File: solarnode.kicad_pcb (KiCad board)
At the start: 2 copper layers, 35.9 x 42.4 mm, 85 parts, among them J1 Conn_01x06, J2 Conn_01x02, J3 Conn_01x02, J4 Conn_01x02, Q1 AO3400, Q4 S8550, Q5 S8050, SW1 3*4*2mm, U1 LM358, U2 OC5864, U3 PY32F003F18U6TR, U4 MAX485E, U5 SGM2033-3.3

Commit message: 设置最小走线宽度，添加一个覆铜区域
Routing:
- added copper zone on F.Cu, net /SLR+
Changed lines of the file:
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@@
+	)
+	(zone
+		(net 2)
+		(net_name "/SLR+")
+		(layer "F.Cu")
+		(hatch edge 0.5)
+		(priority 2)
+		(connect_pads
+			(clearance 0.5)
+		)
+		(min_thickness 0.25)
+		(filled_areas_thickness no)
+		(fill
+			(thermal_gap 0.5)
+			(thermal_bridge_width 0.5)
+		)
+		(polygon
+			(pts
+				(xy 120.72 74.08) (xy 125.07 74.07) (xy 125.07 77.51) (xy 124.13 77.51)
+			)
+		)
 	)
 	(zone
@@
 		(members "0b195e1f-babf-4dd7-9778-632fff0e3cce" "0b9fd526-c495-4a28-b2e9-279cccde64c3"
 			"0cb29699-525d-4bef-8c6a-afe7e7c22e20" "10d58e8f-0aad-4bec-bd13-2f00d2747619"
-			"1c242126-39b0-447e-830a-f3419bd5cad9" "25452366-fbd4-4985-bb02-c5ece706e4f4"
-			"27b9df76-6cdb-48db-b4f1-e2f8790ba447" "28aaa7e5-87bc-432f-b25e-acfecf6c6762"
-			"2f6ba13a-da92-4fc3-804b-7dc0fc54600a" "3cfbca58-6908-402c-8276-13622b5ffac9"
-			"4275d5b1-ca27-4961-b031-94b2a6b556a3" "452a51fe-f178-469a-a51a-106b8d1dc850"
-			"51f7e861-3757-4698-89f5-b66a34f994b3" "58c3f5fa-2f3d-4d57-825c-d2c1d860c3b2"
-			"5941b24d-1f63-45ff-967a-e51922289169" "5a586efe-4cbd-4fc6-b4a6-e8dbcd59427e"
-			"5f12d628-a1dd-4db5-938a-4d464c3aa2ad" "6415759b-c2e6-4038-8d28-fc3f17af7cc9"
-			"6ba225a6-c6fd-4747-89fa-a114a3a3d984" "6f81ba97-3f2b-443c-96c2-e10cbbdcc9ac"
-			"7b04d5f7-4c74-4899-b87d-20ca741adffe" "7fd1d17c-de07-4936-b434-a1391bb95d6b"
+			"1c242126-39b0-447e-830a-f3419bd5cad9" "204c7967-4432-440b-a5a2-ccb7b2b515f3"
+			"25452366-fbd4-4985-bb02-c5ece706e4f4" "27b9df76-6cdb-48db-b4f1-e2f8790ba447"
+			"28aaa7e5-87bc-432f-b25e-acfecf6c6762" "2f6ba13a-da92-4fc3-804b-7dc0fc54600a"
+			"3cfbca58-6908-402c-8276-13622b5ffac9" "4275d5b1-ca27-4961-b031-94b2a6b556a3"
+			"452a51fe-f178-469a-a51a-106b8d1dc850" "51f7e861-3757-4698-89f5-b66a34f994b3"
+			"58c3f5fa-2f3d-4d57-825c-d2c1d860c3b2" "5941b24d-1f63-45ff-967a-e51922289169"
+			"5a586efe-4cbd-4fc6-b4a6-e8dbcd59427e" "5f12d628-a1dd-4db5-938a-4d464c3aa2ad"
+			"6415759b-c2e6-4038-8d28-fc3f17af7cc9" "6ba225a6-c6fd-4747-89fa-a114a3a3d984"
+			"6f81ba97-3f2b-443c-96c2-e10cbbdcc9ac" "7b04d5f7-4c74-4899-b87d-20ca741adffe"
+			"7fd1d17c-de07-4936-b434-a1391bb95d6b" "804d4bcb-e463-4575-b1d0-e9075123a17c"
 			"80c44cac-9446-4b06-b20b-3ae549fe4b68" "88546c8c-a9af-4307-93a9-23e95cf7837e"
 			"8cda7904-a0ac-4ade-8034-a40ec37bfcb2" "ae562753-035c-49e5-87da-800e1a1d988c"

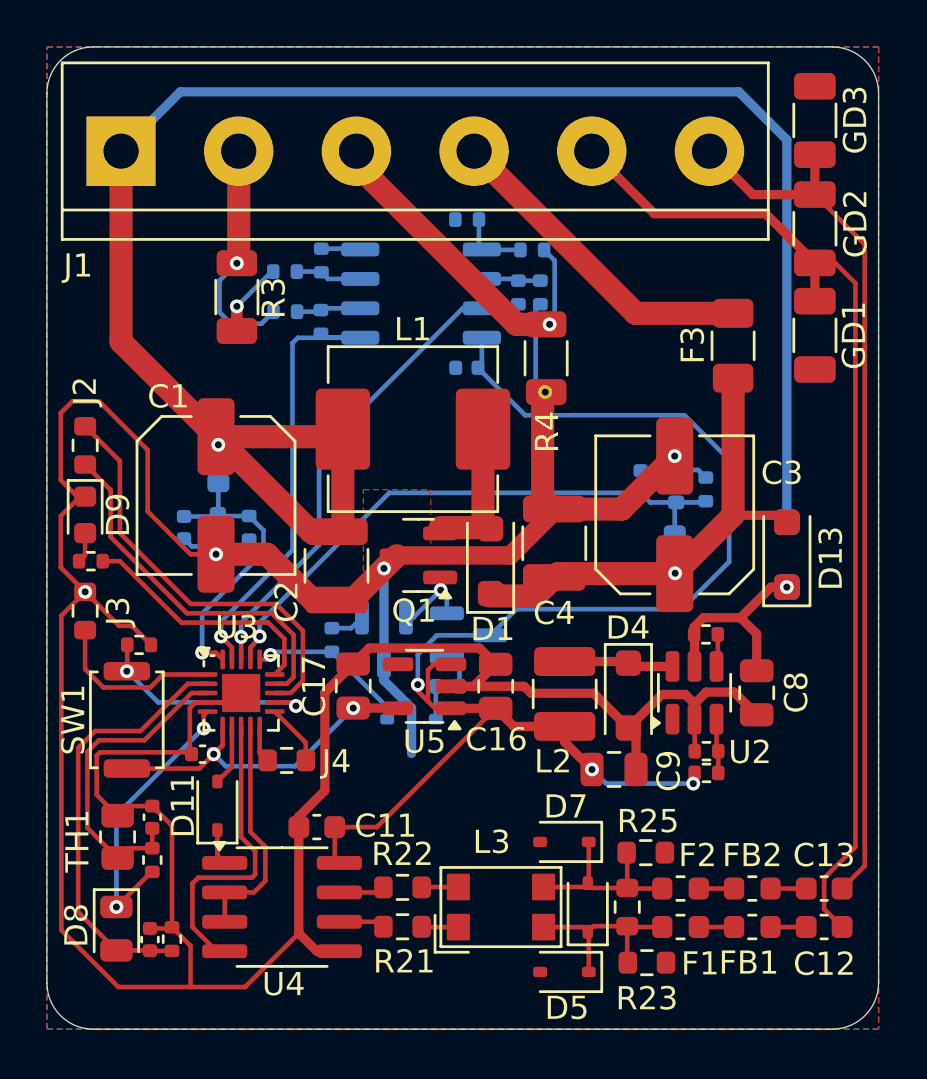
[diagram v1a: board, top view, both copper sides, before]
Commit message: 优化GND连接，添加过孔，调整走线
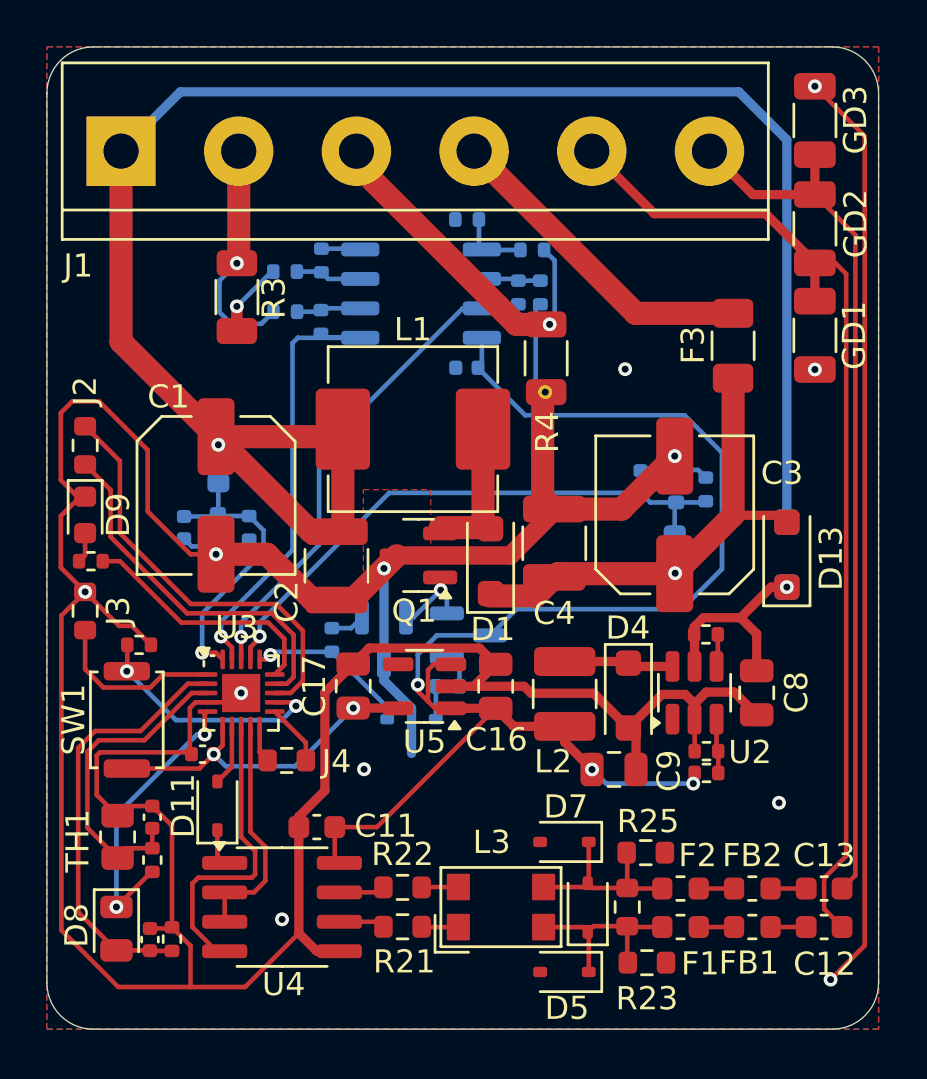
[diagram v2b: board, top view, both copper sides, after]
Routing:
- net GND: track 162.1 -> 202.1 mm, vias 4 -> 12
- net /PUSH: track 10.1 -> 10.6 mm

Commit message: 微调：适当加粗电源走线，添加过孔
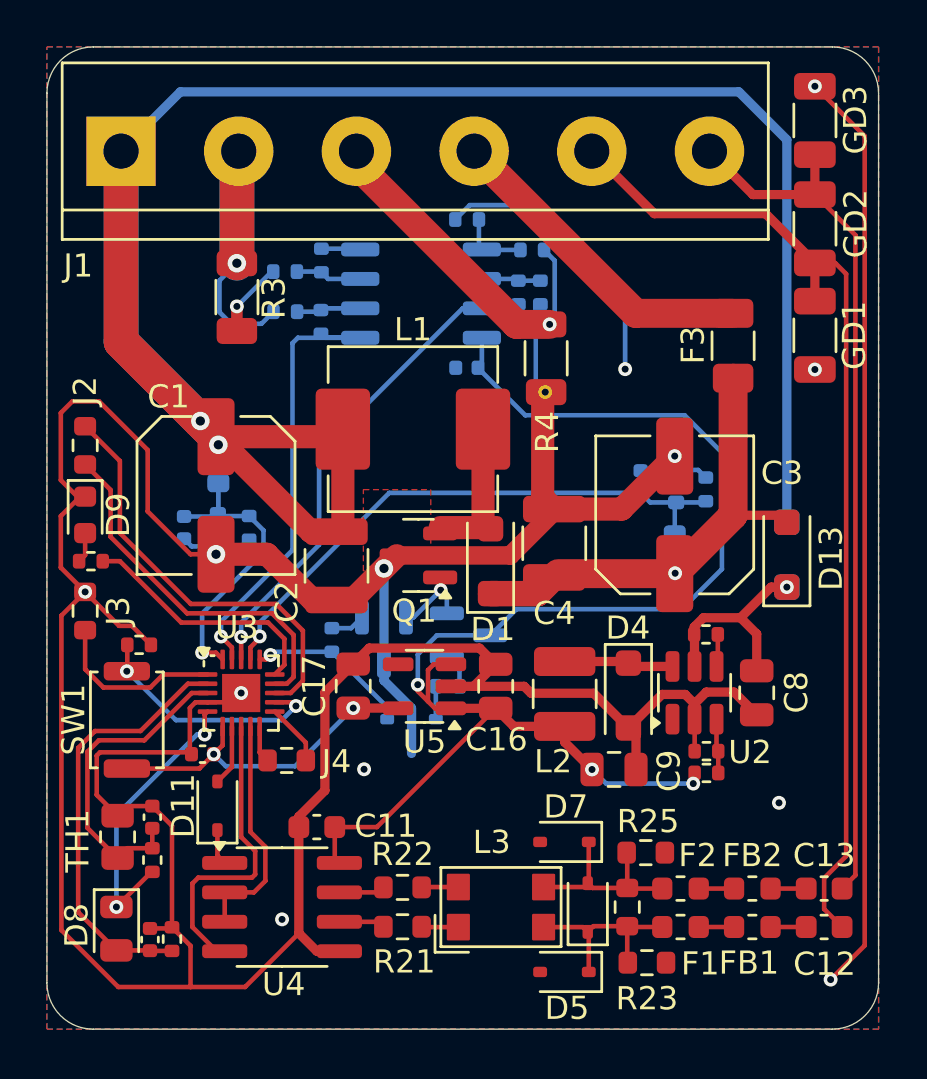
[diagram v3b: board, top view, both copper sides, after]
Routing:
- net /SLR+: track 78.0 -> 92.8 mm, vias 1 -> 2
- net GND: track 202.1 -> 214.7 mm
- net /SLR-: track 10.0 -> 14.9 mm
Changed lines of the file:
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@@
 	(via
 		(at 119.9 78.8)
-		(size 0.6)
-		(drill 0.3)
+		(size 0.8)
+		(drill 0.4)
 		(layers "F.Cu" "B.Cu")
 		(net 1)
@@
 	(via
 		(at 127.15 79.4125)
-		(size 0.6)
-		(drill 0.3)
+		(size 0.8)
+		(drill 0.4)
 		(layers "F.Cu" "B.Cu")
 		(free yes)
@@
 	)
 	(segment
+		(start 130.85 63.73)
+		(end 133.98 63.73)
+		(width 0.2)
+		(layer "B.Cu")
+		(net 1)
+	)
+	(segment
+		(start 137.56 67.31)
+		(end 137.56 70.81)
+		(width 0.2)
+		(layer "B.Cu")
+		(net 1)
+	)
+	(segment
 		(start 127.15 84.25)
 		(end 128.34 85.44)
@@
 	)
 	(segment
+		(start 130.23 64.35)
+		(end 130.85 63.73)
+		(width 0.2)
+		(layer "B.Cu")
+		(net 1)
+	)
+	(segment
 		(start 128.34 85.44)
 		(end 128.34 87.4)
@@
 		(start 140.71 75.16)
 		(end 141.04 75.49)
+		(width 0.2)
+		(layer "B.Cu")
+		(net 1)
+	)
+	(segment
+		(start 133.98 63.73)
+		(end 137.56 67.31)
 		(width 0.2)
 		(layer "B.Cu")
@@
 	)
 	(segment
-		(start 119.9 73.725)
-		(end 115.8 69.625)
-		(width 1)
+		(start 115.8 69.625)
+		(end 115.8 61.4)
+		(width 1.5)
 		(layer "F.Cu")
 		(net 2)
@@
 	)
 	(segment
+		(start 120 73.825)
+		(end 120 74.075)
+		(width 1.5)
+		(layer "F.Cu")
+		(net 2)
+	)
+	(segment
+		(start 119.2225 73.0475)
+		(end 120 73.825)
+		(width 1.5)
+		(layer "F.Cu")
+		(net 2)
+	)
+	(segment
 		(start 125.375 73.4)
 		(end 125.375 77.55)
@@
 	)
 	(segment
+		(start 119.2225 73.0475)
+		(end 115.8 69.625)
+		(width 1.5)
+		(layer "F.Cu")
+		(net 2)
+	)
+	(via
+		(at 120 74.075)
+		(size 0.8)
+		(drill 0.4)
+		(layers "F.Cu" "B.Cu")
+		(net 2)
+	)
+	(via
+		(at 119.2225 73.0475)
+		(size 0.8)
+		(drill 0.4)
+		(layers "F.Cu" "B.Cu")
+		(net 2)
+	)
+	(segment
+		(start 119.2225 73.0475)
+		(end 115.8 69.625)
+		(width 1.5)
+		(layer "B.Cu")
+		(net 2)
+	)
+	(segment
+		(start 120 73.825)
+		(end 119.2225 73.0475)
+		(width 1.5)
+		(layer "B.Cu")
+		(net 2)
+	)
+	(segment
+		(start 142.47 58.84)
+		(end 118.36 58.84)
+		(width 0.4)
+		(layer "B.Cu")
+		(net 2)
+	)
+	(segment
+		(start 144.54 77.4175)
+		(end 144.54 60.91)
+		(width 0.4)
+		(layer "B.Cu")
+		(net 2)
+	)
+	(segment
+		(start 144.54 60.91)
+		(end 142.47 58.84)
+		(width 0.4)
+		(layer "B.Cu")
+		(net 2)
+	)
+	(segment
+		(start 118.36 58.84)
+		(end 115.8 61.4)
+		(width 0.4)
+		(layer "B.Cu")
+		(net 2)
+	)
+	(segment
 		(start 115.8 69.625)
 		(end 115.8 61.4)
+		(width 1.5)
+		(layer "B.Cu")
+		(net 2)
+	)
+	(segment
+		(start 120 74.075)
+		(end 120 73.825)
 		(width 1)
-		(layer "F.Cu")
-		(net 2)
-	)
-	(via
-		(at 120 74.075)
-		(size 0.6)
-		(drill 0.3)
-		(layers "F.Cu" "B.Cu")
-		(net 2)
-	)
-	(segment
-		(start 142.47 58.84)
-		(end 118.36 58.84)
-		(width 0.4)
-		(layer "B.Cu")
-		(net 2)
-	)
-	(segment
-		(start 144.54 77.4175)
-		(end 144.54 60.91)
-		(width 0.4)
-		(layer "B.Cu")
-		(net 2)
-	)
-	(segment
-		(start 144.54 60.91)
-		(end 142.47 58.84)
-		(width 0.4)
-		(layer "B.Cu")
-		(net 2)
-	)
-	(segment
-		(start 118.36 58.84)
-		(end 115.8 61.4)
-		(width 0.4)
 		(layer "B.Cu")
 		(net 2)
@@
 		(start 131.04 61.43)
 		(end 138.01 68.4)
-		(width 1)
+		(width 1.25)
 		(layer "F.Cu")
 		(net 21)
@@
 		(start 138.01 68.4)
 		(end 142.22 68.4)
-		(width 1)
+		(width 1.25)
 		(layer "F.Cu")
 		(net 21)
@@
 	)
 	(segment
-		(start 120.88 66.1575)
-		(end 120.8 66.2375)
-		(width 0.4)
+		(start 120.8 61.47)
+		(end 120.88 61.4)
+		(width 1.5)
 		(layer "F.Cu")
 		(net 30)
 	)
 	(segment
-		(start 120.88 61.4)
-		(end 120.88 66.1575)
-		(width 1)
+		(start 120.8 66.2275)
+		(end 120.8 61.47)
+		(width 1.5)
 		(layer "F.Cu")
 		(net 30)
@@
 	(via
 		(at 120.8 66.2375)
-		(size 0.6)
-		(drill 0.3)
+		(size 0.8)
+		(drill 0.4)
 		(layers "F.Cu" "B.Cu")
 		(net 30)
 	)
 	(segment
+		(start 120.8 61.48)
+		(end 120.88 61.4)
+		(width 1.5)
+		(layer "B.Cu")
+		(net 30)
+	)
+	(segment
+		(start 120.8 66.2375)
+		(end 120.8 61.48)
+		(width 1.5)
+		(layer "B.Cu")
+		(net 30)
+	)
+	(segment
+		(start 120.55 68.85)
+		(end 121.86 68.85)
+		(width 0.2)
+		(layer "B.Cu")
+		(net 30)
+	)
+	(segment
 		(start 121.86 68.85)
+		(end 122.38 68.33)
+		(width 0.2)
+		(layer "B.Cu")
+		(net 30)
+	)
+	(segment
+		(start 120.05 66.9875)
+		(end 120.05 68.35)
+		(width 0.2)
+		(layer "B.Cu")
+		(net 30)
+	)
+	(segment
+		(start 120.05 68.35)
 		(end 120.55 68.85)
 		(width 0.2)
@@
 	)
 	(segment
-		(start 120.55 68.85)
-		(end 120.05 68.35)
-		(width 0.2)
-		(layer "B.Cu")
-		(net 30)
-	)
-	(segment
-		(start 122.38 68.33)
-		(end 121.86 68.85)
-		(width 0.2)
-		(layer "B.Cu")
-		(net 30)
-	)
-	(segment
-		(start 120.05 68.35)
+		(start 120.8 66.2375)
 		(end 120.05 66.9875)
-		(width 0.2)
-		(layer "B.Cu")
-		(net 30)
-	)
-	(segment
-		(start 120.05 66.9875)
-		(end 120.8 66.2375)
 		(width 0.2)
 		(layer "B.Cu")
@@
 		(start 125.96 61.965)
 		(end 125.96 61.4)
-		(width 1)
+		(width 1.25)
 		(layer "F.Cu")
 		(net 31)
@@
 		(start 132.8725 68.8775)
 		(end 125.96 61.965)
-		(width 1)
+		(width 1.25)
 		(layer "F.Cu")
 		(net 31)
@@
 		(start 134.3 68.8775)
 		(end 132.8725 68.8775)
-		(width 1)
+		(width 1.25)
 		(layer "F.Cu")
 		(net 31)
@@
 	)
 	(segment
-		(start 131.7 80.6)
-		(end 133.7 80.6)
-		(width 1)
-		(layer "F.Cu")
-		(net 57)
-	)
-	(segment
-		(start 133.7 80.6)
-		(end 134.5 79.8)
-		(width 1)
+		(start 131.75 80.5)
+		(end 133.8 80.5)
+		(width 1.1)
 		(layer "F.Cu")
 		(net 57)
@@
 	)
 	(segment
+		(start 133.8 80.5)
+		(end 134.5 79.8)
+		(width 1.1)
+		(layer "F.Cu")
+		(net 57)
+	)
+	(segment
 		(start 144.24 77.1175)
 		(end 144.54 77.4175)
@@
 		(start 139.7 79.6375)
 		(end 134.6625 79.6375)
-		(width 1)
+		(width 1.25)
 		(layer "F.Cu")
 		(net 57)
@@
 		(start 142.22 71.2)
 		(end 142.22 77.1175)
-		(width 1)
+		(width 1.25)
 		(layer "F.Cu")
 		(net 57)
@@
 		(start 142.22 77.1175)
 		(end 139.7 79.6375)
-		(width 1)
+		(width 1.25)
 		(layer "F.Cu")
 		(net 57)
@@
 	)
 	(group ""
-		(members "0b195e1f-babf-4dd7-9778-632fff0e3cce" "0b9fd526-c495-4a28-b2e9-279cccde64c3"
+		(members "03b5f41d-5c03-4839-8296-d8cd43c0627e" "0b195e1f-babf-4dd7-9778-632fff0e3cce"
 			"0cb29699-525d-4bef-8c6a-afe7e7c22e20" "10d58e8f-0aad-4bec-bd13-2f00d2747619"
 			"1c242126-39b0-447e-830a-f3419bd5cad9" "204c7967-4432-440b-a5a2-ccb7b2b515f3"
-			"25452366-fbd4-4985-bb02-c5ece706e4f4" "27b9df76-6cdb-48db-b4f1-e2f8790ba447"
-			"28aaa7e5-87bc-432f-b25e-acfecf6c6762" "2f6ba13a-da92-4fc3-804b-7dc0fc54600a"
-			"3cfbca58-6908-402c-8276-13622b5ffac9" "4275d5b1-ca27-4961-b031-94b2a6b556a3"
-			"452a51fe-f178-469a-a51a-106b8d1dc850" "51f7e861-3757-4698-89f5-b66a34f994b3"
+			"27b9df76-6cdb-48db-b4f1-e2f8790ba447" "28aaa7e5-87bc-432f-b25e-acfecf6c6762"
+			"2f6ba13a-da92-4fc3-804b-7dc0fc54600a" "3cfbca58-6908-402c-8276-13622b5ffac9"
+			"4275d5b1-ca27-4961-b031-94b2a6b556a3" "452a51fe-f178-469a-a51a-106b8d1dc850"
+			"51f7e861-3757-4698-89f5-b66a34f994b3" "57f60d52-88cd-409a-94db-b9abf0bc1f31"
 			"58c3f5fa-2f3d-4d57-825c-d2c1d860c3b2" "5941b24d-1f63-45ff-967a-e51922289169"
 			"5a586efe-4cbd-4fc6-b4a6-e8dbcd59427e" "5f12d628-a1dd-4db5-938a-4d464c3aa2ad"

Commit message: 添加接口定义丝印标识
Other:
- board text added: "- 485 + | + BUS - | - SLR +"
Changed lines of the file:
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@@
+		)
+	)
+	(gr_text "- 485 +  |  + BUS -  |  - SLR +"
+		(at 141.78 59.22 0)
+		(layer "B.SilkS")
+		(effects
+			(font
+				(size 0.92 0.92)
+				(thickness 0.1)
+			)
+			(justify left bottom mirror)
 		)
 	)

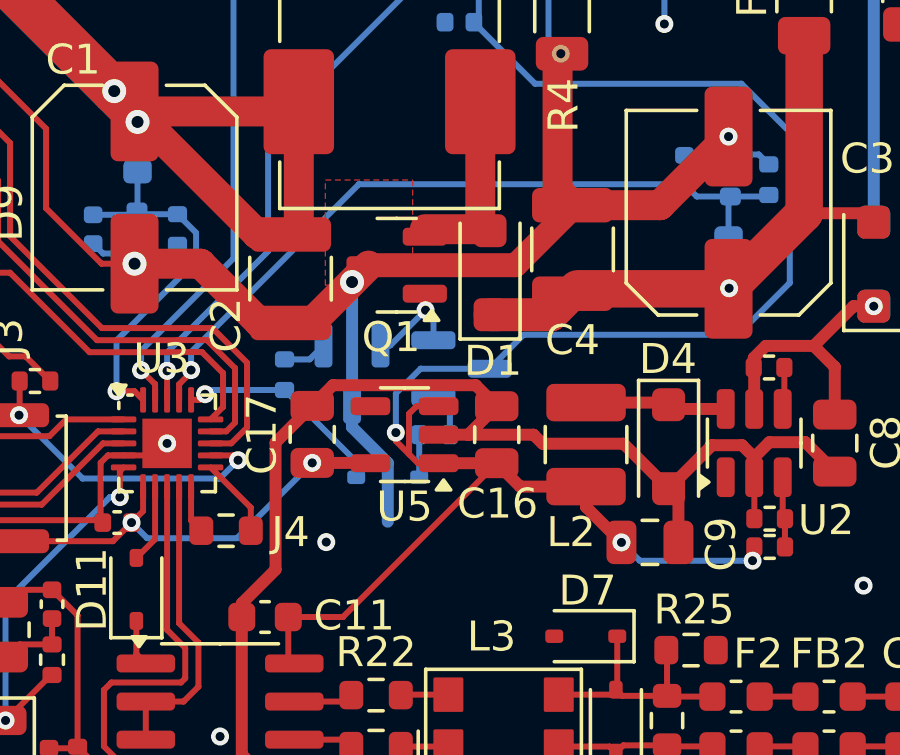
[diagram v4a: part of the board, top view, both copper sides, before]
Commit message: fix: 修复MOS管引脚错误，MOS_DrvIn添加上拉电阻避免上电时烧毁MOS
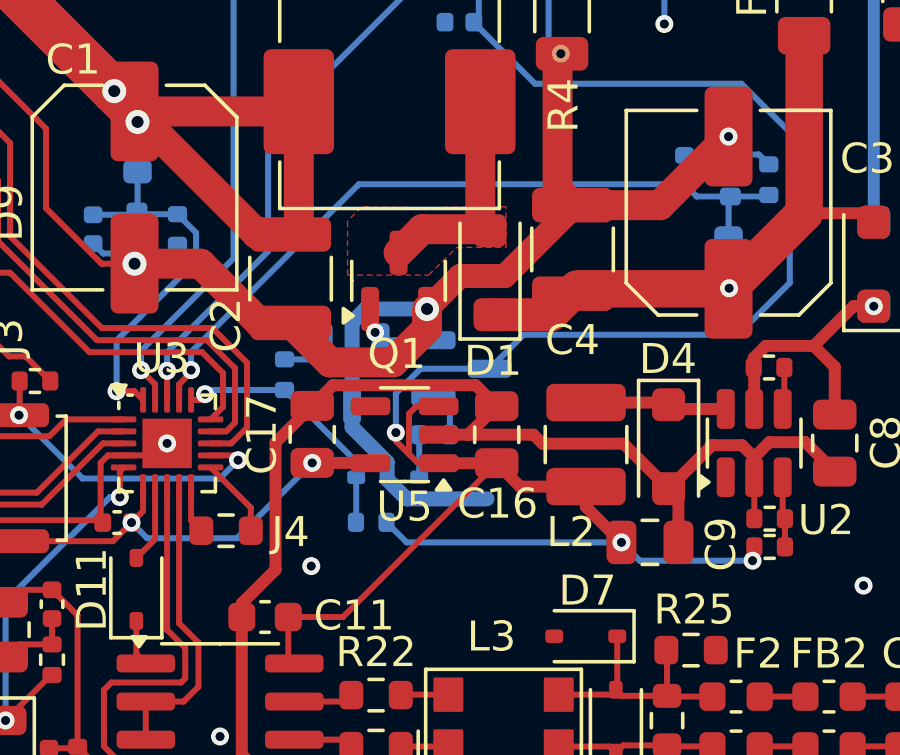
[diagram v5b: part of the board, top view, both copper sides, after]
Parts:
- added R29: 10k, Resistor_SMD:R_0402_1005Metric, B.Cu at (127.8, 87.4)
- D10: value 2.0V -> ~
- moved Q1 0.53 mm to (128.7, 79.4), turned to 90 degrees
- turned D10 to 0 degrees
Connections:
- D10 pad 1: Net-(D10-K) -> /MOS_DrvIn
- D10 pad 2: /MOS_DrvIn -> Net-(D10-A)
- Q1 pad 2: Net-(D1-A) -> GND
- Q1 pad 3: GND -> Net-(D1-A)
- R1 pad 1: Net-(D10-K) -> Net-(D10-A)
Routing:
- net +5V: track 62.3 -> 70.4 mm
- net GND: track 214.7 -> 220.4 mm
- net /MOS_DrvIn: track 7.15 -> 8.72 mm
- net Net-(D10-K): track 1.42 -> 0.00 mm
- net Net-(D10-A): track 0.00 -> 1.42 mm
- net Net-(D1-A): track 6.20 -> 7.40 mm
- net /MOS_G: track 3.66 -> 2.90 mm
- added copper zone on F.Cu, net Net-(D1-A)
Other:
- board text added: "SolarNode Photovoltaic Controll 2025.11.11 v1.0-g52c6c4c Copyright (C) 2025 Xu Ruijun License under CERN-OHL-S v2"
- board text removed: "SolarNode Photovoltaic Controll yyyy.mm.dd vx.x-gxxxxxxx Copyright (C) 2025 Xu Ruijun License under CERN-OHL-S v2"
